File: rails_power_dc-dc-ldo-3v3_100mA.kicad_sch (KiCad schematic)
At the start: 4 parts, among them U101 HT75xx-1-SOT89

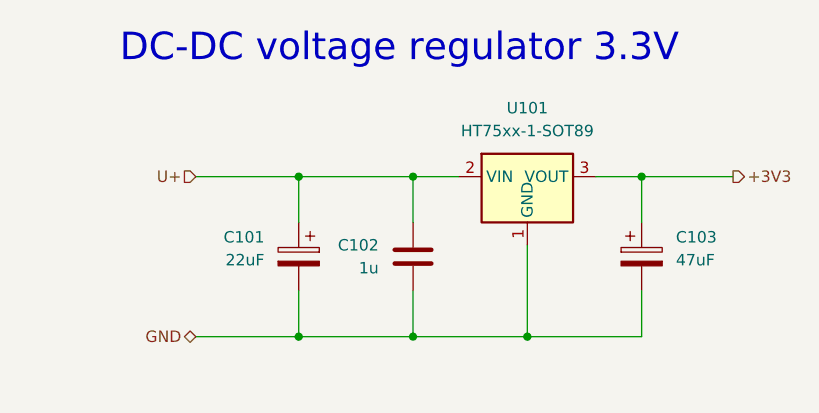
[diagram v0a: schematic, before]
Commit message: Fix - DRC errors in LDO test schematics
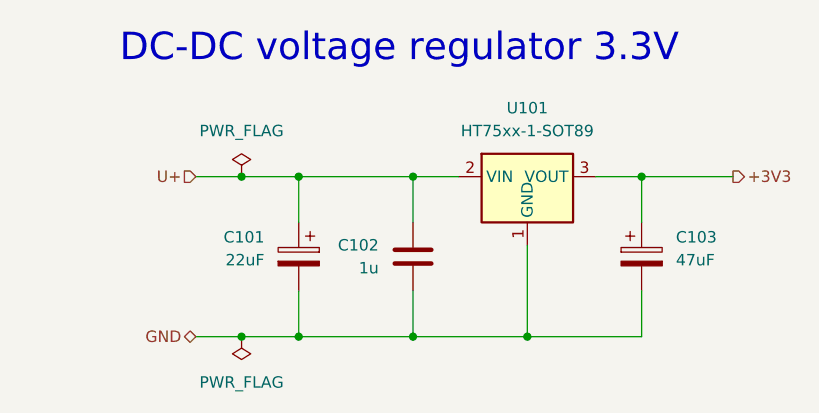
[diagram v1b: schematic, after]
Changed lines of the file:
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@@
+	)
+	(junction
+		(at 44.45 41.91)
+		(diameter 0)
+		(color 0 0 0 0)
 	)
 	(junction
@@
 	)
 	(junction
+		(at 44.45 59.69)
+		(diameter 0)
+		(color 0 0 0 0)
+	)
+	(junction
 		(at 88.9 41.91)
 		(diameter 0)
@@
 	(wire
 		(pts
-			(xy 39.37 59.69) (xy 50.8 59.69)
+			(xy 39.37 59.69) (xy 44.45 59.69)
+		)
+		(stroke
+			(width 0)
+			(type default)
+		)
+	)
+	(wire
+		(pts
+			(xy 44.45 59.69) (xy 50.8 59.69)
+		)
+		(stroke
+			(width 0)
+			(type default)
+		)
+	)
+	(wire
+		(pts
+			(xy 44.45 41.91) (xy 50.8 41.91)
 		)
 		(stroke
@@
 	(wire
 		(pts
-			(xy 39.37 41.91) (xy 50.8 41.91)
+			(xy 39.37 41.91) (xy 44.45 41.91)
 		)
 		(stroke
@@
 					(unit 1)
 				)
+				(path "/0ed6639a-cde6-4452-b9e1-77c370bade86/f74e307f-98ea-4a21-90fe-788ab4c41003"
+					(reference "C203")
+					(unit 1)
+				)
 			)
 			(project "acc-rp2040-baseboard"
@@
 				(path "/e8f9fd83-27d4-40ee-a2c1-fd6356795d83/74710df9-7e61-48be-b0f8-0d4cba0f15c2/a5aa2612-0bfe-49ce-a543-ccf125bffe47"
 					(reference "C?")
-					(unit 1)
-				)
-			)
-			(project "rails_power_dc-dc-ldo-3v3_100mA-test"
-				(path "/fb33ec4e-6596-45d2-a121-8d3475acd69a/a3f567b3-edcb-4aa0-8471-532dbe641db4"
-					(reference "C203")
 					(unit 1)
 				)
@@
 					(unit 1)
 				)
+				(path "/0ed6639a-cde6-4452-b9e1-77c370bade86/f74e307f-98ea-4a21-90fe-788ab4c41003"
+					(reference "C201")
+					(unit 1)
+				)
 			)
 			(project "acc-rp2040-baseboard"
@@
 				)
 			)
+		)
+	)
+	(symbol
+		(lib_id "power:PWR_FLAG")
+		(at 44.45 59.69 0)
+		(mirror x)
+		(unit 1)
+		(exclude_from_sim no)
+		(in_bom yes)
+		(on_board yes)
+		(dnp no)
+		(property "Reference" "#FLG202"
+			(at 44.45 61.595 0)
+			(effects
+				(font
+					(size 1.27 1.27)
+				)
+				(hide yes)
+			)
+		)
+		(property "Value" "PWR_FLAG"
+			(at 44.45 64.77 0)
+			(effects
+				(font
+					(size 1.27 1.27)
+				)
+			)
+		)
+		(property "Footprint" ""
+			(at 44.45 59.69 0)
+			(effects
+				(font
+					(size 1.27 1.27)
+				)
+				(hide yes)
+			)
+		)
+		(property "Datasheet" "~"
+			(at 44.45 59.69 0)
+			(effects
+				(font
+					(size 1.27 1.27)
+				)
+				(hide yes)
+			)
+		)
+		(property "Description" "Special symbol for telling ERC where power comes from"
+			(at 44.45 59.69 0)
+			(effects
+				(font
+					(size 1.27 1.27)
+				)
+				(hide yes)
+			)
+		)
+		(pin "1"
+		)
+		(instances
 			(project "rails_power_dc-dc-ldo-3v3_100mA-test"
-				(path "/fb33ec4e-6596-45d2-a121-8d3475acd69a/a3f567b3-edcb-4aa0-8471-532dbe641db4"
-					(reference "C201")
+				(path "/0ed6639a-cde6-4452-b9e1-77c370bade86/f74e307f-98ea-4a21-90fe-788ab4c41003"
+					(reference "#FLG202")
 					(unit 1)
 				)
@@
 					(unit 1)
 				)
+				(path "/0ed6639a-cde6-4452-b9e1-77c370bade86/f74e307f-98ea-4a21-90fe-788ab4c41003"
+					(reference "U201")
+					(unit 1)
+				)
 			)
 			(project "acc-rp2040-baseboard"
@@
 				(path "/e8f9fd83-27d4-40ee-a2c1-fd6356795d83/74710df9-7e61-48be-b0f8-0d4cba0f15c2/a5aa2612-0bfe-49ce-a543-ccf125bffe47"
 					(reference "U?")
-					(unit 1)
-				)
-			)
-			(project "rails_power_dc-dc-ldo-3v3_100mA-test"
-				(path "/fb33ec4e-6596-45d2-a121-8d3475acd69a/a3f567b3-edcb-4aa0-8471-532dbe641db4"
-					(reference "U201")
 					(unit 1)
 				)
@@
 					(unit 1)
 				)
+				(path "/0ed6639a-cde6-4452-b9e1-77c370bade86/f74e307f-98ea-4a21-90fe-788ab4c41003"
+					(reference "C202")
+					(unit 1)
+				)
 			)
 			(project "acc-rp2040-baseboard"
@@
 				)
 			)
-			(project "rails_power_dc-dc-ldo-3v3_100mA-test"
-				(path "/fb33ec4e-6596-45d2-a121-8d3475acd69a/a3f567b3-edcb-4aa0-8471-532dbe641db4"
-					(reference "C202")
-					(unit 1)
-				)
+		)
+	)
+	(symbol
+		(lib_id "power:PWR_FLAG")
+		(at 44.45 41.91 0)
+		(unit 1)
+		(exclude_from_sim no)
+		(in_bom yes)
+		(on_board yes)
+		(dnp no)
+		(fields_autoplaced yes)
+		(property "Reference" "#FLG201"
+			(at 44.45 40.005 0)
+			(effects
+				(font
+					(size 1.27 1.27)
+				)
+				(hide yes)
+			)
+		)
+		(property "Value" "PWR_FLAG"
+			(at 44.45 36.83 0)
+			(effects
+				(font
+					(size 1.27 1.27)
+				)
+			)
+		)
+		(property "Footprint" ""
+			(at 44.45 41.91 0)
+			(effects
+				(font
+					(size 1.27 1.27)
+				)
+				(hide yes)
+			)
+		)
+		(property "Datasheet" "~"
+			(at 44.45 41.91 0)
+			(effects
+				(font
+					(size 1.27 1.27)
+				)
+				(hide yes)
+			)
+		)
+		(property "Description" "Special symbol for telling ERC where power comes from"
+			(at 44.45 41.91 0)
+			(effects
+				(font
+					(size 1.27 1.27)
+				)
+				(hide yes)
+			)
+		)
+		(pin "1"
+		)
+		(instances
+			(project ""
+				(path "/0ed6639a-cde6-4452-b9e1-77c370bade86/f74e307f-98ea-4a21-90fe-788ab4c41003"
+					(reference "#FLG201")
+					(unit 1)
+				)
